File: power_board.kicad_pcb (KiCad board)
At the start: 2 copper layers, 141 x 90 mm, 172 parts, among them CON1 MICROUSB, J1 Conn_02x03_Odd_Even, J10 Conn_01x02, J11 Conn_01x02, J12 Conn_01x02, J13 Conn_01x02, J14 Conn_01x02, J15 Conn_01x02, J16 Conn_01x02, J17 Conn_01x02, J18 Conn_01x02, J19 Conn_01x02, J2 Conn_01x01, J20 Conn_01x02, J21 Conn_01x03, J22 Conn_01x03, J23 Conn_01x03, J24 Conn_01x03, J25 Conn_01x03, J26 Conn_01x02, J27 Conn_01x02, J28 Conn_01x02, J29 Conn_01x02, J3 Conn_01x01, J30 Conn_01x02, J31 Conn_01x02, J32 Conn_01x02, J33 Conn_01x02, J4 Conn_01x01, J5 ATX-24, J6 Conn_01x02, J7 Conn_01x02, J8 Conn_01x02, J9 Conn_01x02, K1 lsts-devices:RELAY_1RT, K2 lsts-devices:RELAY_1RT, K3 lsts-devices:RELAY_1RT, K4 lsts-devices:RELAY_1RT, K5 lsts-devices:RELAY_1RT, Q1 MMBT4401-7-F, Q10 MMBT4401-7-F, Q11 SI7113ADN-T1-GE3, Q12 MMBT4401-7-F, Q13 MMBT4401-7-F, Q14 MMBT4401-7-F, Q15 SI7113ADN-T1-GE3, Q16 SI7113ADN-T1-GE3, Q17 SI7113ADN-T1-GE3, Q18 MMBT4401-7-F, Q19 MMBT4401-7-F, Q2 MMBT4401-7-F, Q20 SI7113ADN-T1-GE3, Q21 SI7113ADN-T1-GE3, Q3 MMBT4401-7-F, Q4 SI7113ADN-T1-GE3, Q5 SI7113ADN-T1-GE3, Q6 MMBT4401-7-F, Q7 MMBT4401-7-F, Q8 SI7113ADN-T1-GE3, Q9 SI7113ADN-T1-GE3, SW1 SW_Push, U1 PCA9685PW, U10 DRV8801PWP, U11 DRV8801PWP, U12 DRV8801PWP, U2 ATMEGA328P-AU, U3 PCA9685PW, U4 FT232RL, U5 DRV8801PWP, U6 DRV8801PWP, U7 DRV8801PWP, U8 DRV8801PWP, U9 DRV8801PWP, Y1 Crystal

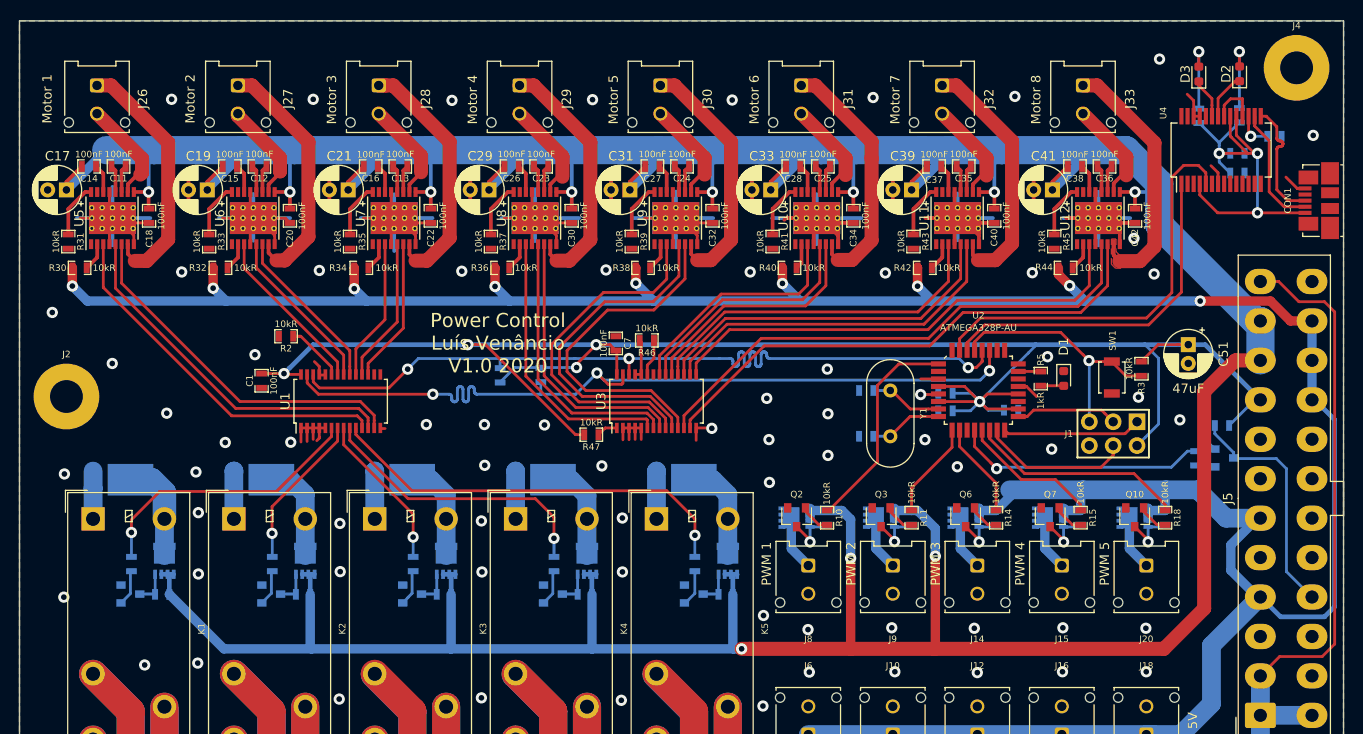
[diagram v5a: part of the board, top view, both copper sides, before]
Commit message: Replaced MCU by Arduino Nano
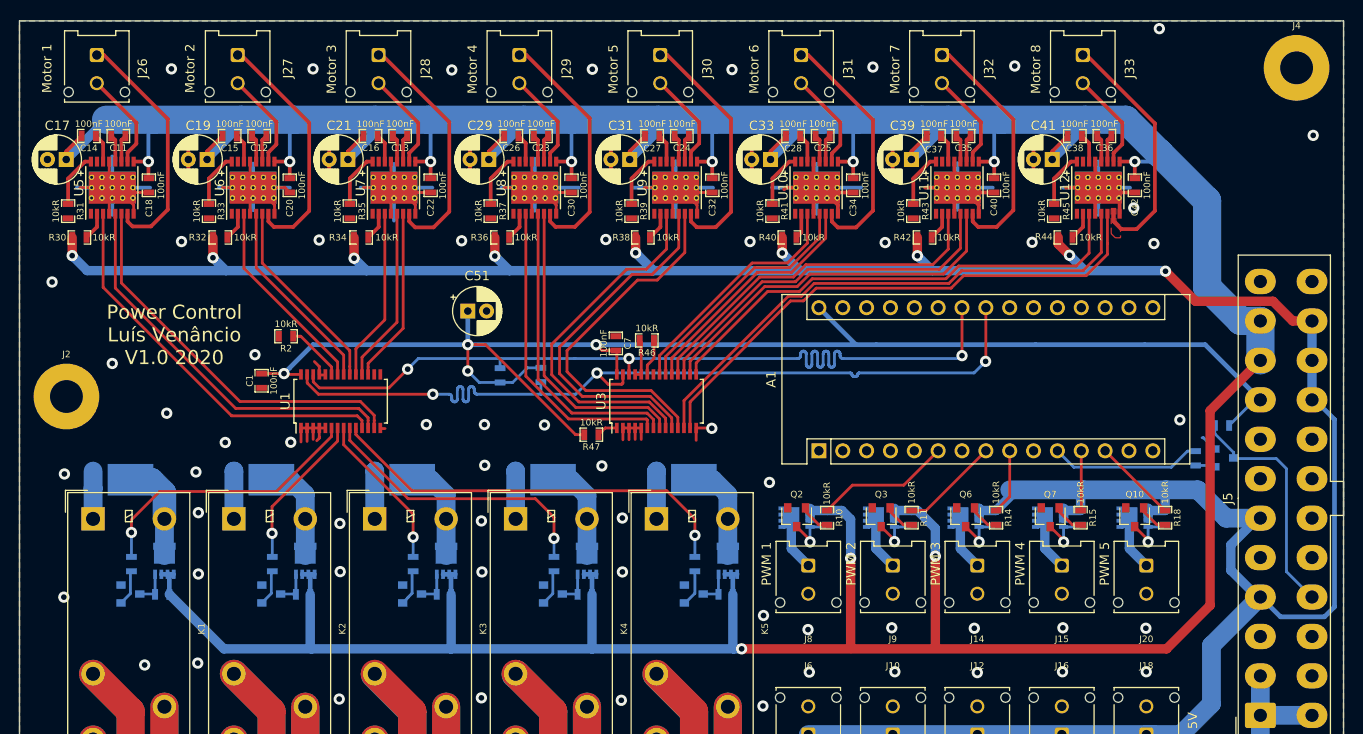
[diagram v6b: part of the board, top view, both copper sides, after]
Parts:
- removed C10, C2, C5, C6, C8, C9: 100nF, lsts-passives:C_0603
- removed C3, C4: 22nF, lsts-passives:C_0603
- removed CON1: MICROUSB, lsts-conn:USB_Micro-B_Molex_47346-0001
- removed D1, D2, D3: LED, LED_SMD:LED_0603_1608Metric
- removed J1: Conn_02x03_Odd_Even, lsts-conn:CONN_ISP
- removed R3: 10kR, lsts-passives:R_0603
- removed R5, R6, R7: 1kR, lsts-passives:R_0603
- removed SW1: SW_Push, Button_Switch_SMD:SW_SPST_B3U-1000P
- removed U2: ATMEGA328P-AU, lsts-ic:TQFP32
- removed U4: FT232RL, Package_SO:SSOP-28_5.3x10.2mm_P0.65mm
- removed Y1: Crystal, Crystal:Crystal_HC49-4H_Vertical
- added A1: Arduino_Nano_v3.x, Module:Arduino_Nano, F.Cu at (165.1, 105.8)
- moved C51 76.8 mm to (127.7, 90.9), turned to 0 degrees
- moved C11 3.24 mm to (90.5, 72.3)
- moved C12 3.24 mm to (105.5, 72.3)
- moved C13 3.24 mm to (120.5, 72.3)
- moved C14 3.24 mm to (87.4, 72.3)
- moved C15 3.24 mm to (102.4, 72.3)
- moved C16 3.24 mm to (117.4, 72.3)
- moved C17 3.24 mm to (85.0, 74.8)
- moved C18 3.24 mm to (93.8, 77.5)
- moved C19 3.24 mm to (100.0, 74.8)
- moved C20 3.24 mm to (108.8, 77.5)
- moved C21 3.24 mm to (115.0, 74.8)
- moved C22 3.24 mm to (123.8, 77.5)
- moved C23 3.24 mm to (135.5, 72.3)
- moved C24 3.24 mm to (150.5, 72.3)
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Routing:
- net +3V3: track 118.1 -> 64.1 mm
- net /+5V_SB: track 204.1 -> 158.6 mm, vias 5 -> 4
- net /5V_USB: track 44.1 -> 0.00 mm, vias 3 -> 0
- net /AT_TXD: track 43.8 -> 0.00 mm
- net /AT_RXD: track 37.4 -> 0.00 mm
- net /RESET: track 27.6 -> 0.00 mm, vias 1 -> 0
- net GND: track 342.9 -> 323.3 mm, vias 79 -> 68
- net /MOSI: track 16.0 -> 0.00 mm
- net /MISO: track 14.8 -> 0.00 mm
- net /PWM5_5V: track 23.1 -> 9.02 mm
- net /D-: track 13.2 -> 0.00 mm
- net /D+: track 13.2 -> 0.00 mm
- net /SCK: track 10.9 -> 0.00 mm
- net /PWR_CTR: track 27.0 -> 16.1 mm, vias 1 -> 0
- net /PWM4_5V: track 15.0 -> 6.39 mm
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
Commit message: Final touches
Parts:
- removed C28, C30, C32, C34, C35, C36, C37, C38, C40, C42: 100nF, lsts-passives:C_0603
- removed C29, C31, C33, C39, C41: 100uF, Capacitor_THT:CP_Radial_D5.0mm_P2.00mm
- removed D6, D7, D8: SDT5100LP5-13, Diode_SMD:D_PowerDI-5
- removed the J25 at (155.3, 146.6)
- removed J31, J32, J33: Conn_01x02, Connector_Molex:Molex_Micro-Fit_3.0_43045-0212_2x01_P3.00mm_Vertical
- removed Q17, Q20, Q21: SI7113ADN-T1-GE3, lsts-discretes:PowerPAK_1212-8
- removed Q18, Q19: MMBT4401-7-F, lsts-discretes:SOT23_BC817
- removed R42, R43, R44, R45, R46: 10kR, lsts-passives:R_0603
- removed U10, U11, U12, U9: DRV8801PWP, Package_SO:HTSSOP-16-1EP_4.4x5mm_P0.65mm_EP3.4x5mm_Mask3x3mm_ThermalVias
- added ?: , , F.Cu at (98.1, 64.9)
- added C10: 100uF, Capacitor_THT:CP_Radial_D5.0mm_P2.00mm, F.Cu at (99.9, 70.5)
- added C17: 100nF, lsts_passives:C_0603, F.Cu at (127.0, 70.5)
- added C4: 100nF, lsts_passives:C_0603, F.Cu at (81.7, 73.7)
- added C5: 100nF, lsts_passives:C_0603, F.Cu at (101.7, 73.7)
- added C6: 100nF, lsts_passives:C_0603, F.Cu at (81.7, 76.3)
- added C7: 100nF, lsts_passives:C_0603, F.Cu at (101.7, 76.3)
- added C9: 100nF, lsts_passives:C_0603, F.Cu at (87.0, 70.5)
- added D1: SDT5100LP5-13, Diode_SMD:D_PowerDI-5, B.Cu at (76.5, 113.0)
- added D2: SDT5100LP5-13, Diode_SMD:D_PowerDI-5, B.Cu at (94.0, 113.0)
- added D3: SDT5100LP5-13, Diode_SMD:D_PowerDI-5, B.Cu at (111.5, 113.0)
- added J20: Conn_01x03, TerminalBlock_Phoenix:TerminalBlock_Phoenix_PT-1,5-3-3.5-H_1x03_P3.50mm_Horizontal, F.Cu at (73.0, 144.0)
- added J26: Conn_01x02, Connector_Molex:Molex_Micro-Fit_3.0_43045-0212_2x01_P3.00mm_Vertical, F.Cu at (108.7, 65.3)
- added R4: 10kR, lsts_passives:R_0603, F.Cu at (126.0, 91.3)
- added R5: 10kR, lsts_passives:R_0603, F.Cu at (169.9, 86.8)
- added R7: 10kR, lsts_passives:R_0603, F.Cu at (169.9, 89.7)
- added U3: DRV8801PWP, Package_SO:HTSSOP-16-1EP_4.4x5mm_P0.65mm_EP3.4x5mm_Mask3x3mm_ThermalVias, F.Cu at (87.2, 74.3)
- added U4: DRV8801PWP, Package_SO:HTSSOP-16-1EP_4.4x5mm_P0.65mm_EP3.4x5mm_Mask3x3mm_ThermalVias, F.Cu at (107.2, 74.3)
- C1, C11, C12, C13, C14, C15, C20, C22, C23, C25, C27: footprint lsts-passives:C_0603 -> lsts_passives:C_0603
- C16, C18, C24, C26: value 100nF -> 100uF; footprint lsts-passives:C_0603 -> Capacitor_THT:CP_Radial_D5.0mm_P2.00mm
- C19, C21: value 100uF -> 100nF; footprint Capacitor_THT:CP_Radial_D5.0mm_P2.00mm -> lsts_passives:C_0603
- C2: renamed from C7; footprint lsts-passives:C_0603 -> lsts_passives:C_0603
- J1: renamed from J2; footprint lsts-mecanical:MountingHole_3.5mm_Pad -> lsts_mecanical:MountingHole_3.5mm_Pad
- J2: renamed from J3; footprint lsts-mecanical:MountingHole_3.5mm_Pad -> lsts_mecanical:MountingHole_3.5mm_Pad
- J3: renamed from J4; footprint lsts-mecanical:MountingHole_3.5mm_Pad -> lsts_mecanical:MountingHole_3.5mm_Pad
- K1, K2, K3, K4, K5: value lsts-devices:RELAY_1RT -> SANYOU_SRD_Form_C; footprint Relay_THT:Relay_SPDT_Panasonic_JW1_FormC_lsts -> Relay_THT:Relay_SPDT_SANYOU_SRD_Series_Form_C
- Q1, Q10, Q2, Q3, Q6, Q7: footprint lsts-discretes:SOT23_BC817 -> lsts_discretes:SOT23_BC817
- Q11, Q4, Q5, Q8, Q9: footprint lsts-discretes:PowerPAK_1212-8 -> lsts_discretes:PowerPAK_1212-8
- Q12, Q13, Q14: value MMBT4401-7-F -> Q_NMOS_GDS; footprint lsts-discretes:SOT23_BC817 -> Package_TO_SOT_SMD:TO-252-2; moved to F.Cu
- Q15, Q16: value SI7113ADN-T1-GE3 -> Q_NMOS_GDS; footprint lsts-discretes:PowerPAK_1212-8 -> Package_TO_SOT_SMD:TO-252-2; moved to F.Cu
- R1, R10, R11, R12, R13, R14, R15, R16, R17, R18, R19, R2, R30, R31, R32, R33, R34, R35, R36, R37, R38, R39, R40, R41, R8, R9: footprint lsts-passives:R_0603 -> lsts_passives:R_0603
- R20, R21: value 10kR -> 600R; footprint lsts-passives:R_0603 -> lsts_passives:R_0603; moved to F.Cu
- R22, R26, R27: value 10kR -> 60kR; footprint lsts-passives:R_0603 -> lsts_passives:R_0603; moved to F.Cu
- R23, R29: value 100kR -> 60kR; footprint lsts-passives:R_0603 -> lsts_passives:R_0603; moved to F.Cu
- R24, R25, R28: value 100kR -> 600R; footprint lsts-passives:R_0603 -> lsts_passives:R_0603; moved to F.Cu
- R3: renamed from R4; footprint lsts-passives:R_0603 -> lsts_passives:R_0603
- R6: renamed from R47; footprint lsts-passives:R_0603 -> lsts_passives:R_0603
- moved C3 71.2 mm to (197.7, 104.3), turned to 90 degrees
- moved C21 66.7 mm to (181.7, 73.7), turned to 270 degrees
- moved A1 57.6 mm to (110.0, 89.2), turned to 270 degrees
- moved C20 53.1 mm to (161.7, 73.7), turned to 270 degrees
- moved U8 52.4 mm to (187.2, 74.3), turned to 180 degrees
- moved C26 47.6 mm to (179.9, 70.5), turned to 180 degrees
- moved U7 47.4 mm to (167.2, 74.3), turned to 180 degrees
- moved C19 47.2 mm to (146.9, 70.5)
- moved C18 46.6 mm to (139.9, 70.5), turned to 180 degrees
- moved C23 46.4 mm to (181.7, 76.3), turned to 0 degrees
- moved U6 42.5 mm to (147.2, 74.3), turned to 180 degrees
- moved R22 41.7 mm to (80.5, 113.0)
- moved D5 41.0 mm to (146.5, 113.0)
- moved J30 40.5 mm to (188.7, 65.3), turned to 270 degrees
- moved C27 39.6 mm to (186.9, 70.5), turned to 180 degrees
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- renumbered C51 to C3, C17 to C8, J11 to J10, J12 to J11, J13 to J12, J14 to J13, J15 to J14, J16 to J15, J17 to J16, J18 to J17, J19 to J18, J20 to J19, J26 to J25, J5 to J4, J6 to J5, J7 to J6, J8 to J7, J9 to J8, J10 to J9, U3 to U2
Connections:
- A1 pad 12: /PWM4_5V -> Net-(A1-Pad12)
- A1 pad 13: /PWM5_5V -> Net-(A1-Pad13)
- A1 pad 6: /PWM1_5V -> Net-(A1-Pad6)
- A1 pad 8: /PWM2_5V -> Net-(A1-Pad8)
- A1 pad 9: /PWM3_5V -> Net-(A1-Pad9)
- C11 pad 1: Net-(C11-Pad1) -> GND
- C11 pad 2: Net-(C11-Pad2) -> +12V
- C16 pad 2: Net-(C16-Pad2) -> GND
- C18 pad 1: GND -> +12V
- C18 pad 2: +12V -> GND
- C19 pad 1: +12V -> GND
- C19 pad 2: GND -> +12V
- C20 pad 1: GND -> Net-(C20-Pad1)
- C20 pad 2: +12V -> Net-(C20-Pad2)
- C21 pad 1: +12V -> Net-(C21-Pad1)
- C21 pad 2: GND -> Net-(C21-Pad2)
- C22 pad 1: GND -> +12V
- C22 pad 2: +12V -> Net-(C22-Pad2)
- C23 pad 1: Net-(C23-Pad1) -> +12V
- C24 pad 1: Net-(C24-Pad1) -> +12V
- C24 pad 2: Net-(C24-Pad2) -> GND
- C25 pad 1: Net-(C25-Pad1) -> GND
- C25 pad 2: Net-(C25-Pad2) -> +12V
- C26 pad 2: Net-(C26-Pad2) -> GND
- C27 pad 1: +12V -> GND
- C27 pad 2: Net-(C27-Pad2) -> +12V
- D4 pad 1: Net-(D4-Pad1) -> +5V
- D4 pad 2: GND -> Net-(D4-Pad2)
- D5 pad 1: Net-(D5-Pad1) -> +5V
- D5 pad 2: GND -> Net-(D5-Pad2)
- J25 pad 1: Net-(J26-Pad1) -> Net-(J25-Pad1)
- J25 pad 2: Net-(J26-Pad2) -> Net-(J25-Pad2)
- K1 pad 1: GND -> Net-(J20-Pad2)
- K1 pad 2: Net-(J21-Pad2) -> Net-(D1-Pad2)
- K1 pad 3: Net-(J21-Pad3) -> Net-(J20-Pad1)
- K1 pad 4: Net-(J21-Pad1) -> Net-(J20-Pad3)
- K1 pad 5: Net-(D4-Pad1) -> +5V
- K2 pad 1: GND -> Net-(J21-Pad2)
- K2 pad 2: Net-(J22-Pad2) -> Net-(D2-Pad2)
- K2 pad 3: Net-(J22-Pad3) -> Net-(J21-Pad1)
- K2 pad 4: Net-(J22-Pad1) -> Net-(J21-Pad3)
- K2 pad 5: Net-(D5-Pad1) -> +5V
- K3 pad 1: GND -> Net-(J22-Pad2)
- K3 pad 2: Net-(J23-Pad2) -> Net-(D3-Pad2)
- K3 pad 3: Net-(J23-Pad3) -> Net-(J22-Pad1)
- K3 pad 4: Net-(J23-Pad1) -> Net-(J22-Pad3)
- K3 pad 5: Net-(D6-Pad1) -> +5V
- K4 pad 1: GND -> Net-(J23-Pad2)
- K4 pad 2: Net-(J24-Pad2) -> Net-(D4-Pad2)
- K4 pad 3: Net-(J24-Pad3) -> Net-(J23-Pad1)
- K4 pad 4: Net-(J24-Pad1) -> Net-(J23-Pad3)
- K4 pad 5: Net-(D7-Pad1) -> +5V
- K5 pad 1: GND -> Net-(J24-Pad2)
- K5 pad 2: Net-(J25-Pad2) -> Net-(D5-Pad2)
- K5 pad 3: Net-(J25-Pad3) -> Net-(J24-Pad1)
- K5 pad 4: Net-(J25-Pad1) -> Net-(J24-Pad3)
- K5 pad 5: Net-(D8-Pad1) -> +5V
- R20 pad 2: Net-(Q12-PadB) -> Net-(Q12-Pad1)
- R21 pad 2: Net-(Q13-PadB) -> Net-(Q13-Pad1)
- R22 pad 1: /RLY3_EN -> GND
- R22 pad 2: Net-(Q14-PadB) -> Net-(Q12-Pad1)
- R23 pad 1: Net-(Q12-PadC) -> GND
- R23 pad 2: +12V -> Net-(Q13-Pad1)
- R24 pad 1: Net-(Q13-PadC) -> /RLY3_EN
- R24 pad 2: +12V -> Net-(Q14-Pad1)
- R25 pad 1: Net-(Q14-PadC) -> /RLY4_EN
- R25 pad 2: +12V -> Net-(Q15-Pad1)
- R26 pad 1: /RLY4_EN -> GND
- R26 pad 2: Net-(Q18-PadB) -> Net-(Q14-Pad1)
- R27 pad 1: /RLY5_EN -> GND
- R27 pad 2: Net-(Q19-PadB) -> Net-(Q15-Pad1)
- R28 pad 1: Net-(Q18-PadC) -> /RLY5_EN
- R28 pad 2: +12V -> Net-(Q16-Pad1)
- R29 pad 1: Net-(Q19-PadC) -> GND
- R29 pad 2: +12V -> Net-(Q16-Pad1)
- U1 pad 11: /MTR1_PH -> /MTR3_PH
- U1 pad 12: /MTR1_SL -> /MTR3_SL
- U1 pad 13: /MTR1_EN -> /MTR3_EN
- U1 pad 17: /MTR3_EN -> /MTR2_EN
- U1 pad 18: /MTR3_SL -> /MTR2_SL
- U1 pad 19: /MTR3_PH -> /MTR2_PH
- U1 pad 20: /MTR2_EN -> /MTR1_EN
- U1 pad 21: /MTR2_SL -> /MTR1_SL
- U1 pad 22: /MTR2_PH -> /MTR1_PH
- U1 pad 24: GND -> Net-(R4-Pad1)
- U2 pad 10: /MTR5_SL -> /PWM2_5V
- U2 pad 11: /MTR5_EN -> /PWM3_5V
- U2 pad 12: /MTR8_SL -> /PWM4_5V
- U2 pad 13: /MTR8_EN -> /PWM5_5V
- U2 pad 15: /MTR8_PH -> /MTR6_EN
- U2 pad 16: /MTR7_EN -> /MTR6_SL
- U2 pad 17: /MTR7_SL -> /MTR6_PH
- U2 pad 18: /MTR7_PH -> /MTR5_EN
- U2 pad 19: /MTR6_EN -> /MTR5_SL
- U2 pad 20: /MTR6_SL -> /MTR5_PH
- U2 pad 21: /MTR6_PH -> Net-(U2-Pad21)
- U2 pad 24: GND -> Net-(R7-Pad1)
- U2 pad 9: /MTR5_PH -> /PWM1_5V
- U5 pad 10: Net-(J26-Pad2) -> Net-(J27-Pad2)
- U5 pad 11: Net-(C11-Pad1) -> Net-(C12-Pad1)
- U5 pad 12: Net-(C11-Pad2) -> Net-(C12-Pad2)
- U5 pad 16: Net-(R31-Pad1) -> Net-(R35-Pad1)
- U5 pad 2: Net-(R30-Pad2) -> Net-(R34-Pad2)
- U5 pad 3: /MTR1_PH -> /MTR3_PH
- U5 pad 5: /MTR1_SL -> /MTR3_SL
- U5 pad 6: /MTR1_EN -> /MTR3_EN
- U5 pad 7: Net-(J26-Pad1) -> Net-(J27-Pad1)
- U6 pad 10: Net-(J27-Pad2) -> Net-(J28-Pad2)
- U6 pad 11: Net-(C12-Pad1) -> Net-(C13-Pad1)
- U6 pad 12: Net-(C12-Pad2) -> Net-(C13-Pad2)
- U6 pad 16: Net-(R33-Pad1) -> Net-(R37-Pad1)
- U6 pad 2: Net-(R32-Pad2) -> Net-(R36-Pad2)
- U6 pad 3: /MTR2_PH -> /MTR4_PH
- U6 pad 5: /MTR2_SL -> /MTR4_SL
- U6 pad 6: /MTR2_EN -> /MTR4_EN
- U6 pad 7: Net-(J27-Pad1) -> Net-(J28-Pad1)
- U7 pad 10: Net-(J28-Pad2) -> Net-(J29-Pad2)
- U7 pad 11: Net-(C13-Pad1) -> Net-(C20-Pad1)
- U7 pad 12: Net-(C13-Pad2) -> Net-(C20-Pad2)
- U7 pad 14: Net-(C16-Pad2) -> Net-(C22-Pad2)
- U7 pad 16: Net-(R35-Pad1) -> Net-(R39-Pad1)
- U7 pad 2: Net-(R34-Pad2) -> Net-(R38-Pad2)
- U7 pad 3: /MTR3_PH -> /MTR5_PH
- U7 pad 5: /MTR3_SL -> /MTR5_SL
- U7 pad 6: /MTR3_EN -> /MTR5_EN
- U7 pad 7: Net-(J28-Pad1) -> Net-(J29-Pad1)
- U8 pad 10: Net-(J29-Pad2) -> Net-(J30-Pad2)
- U8 pad 11: Net-(C23-Pad1) -> Net-(C21-Pad1)
- U8 pad 12: Net-(C23-Pad2) -> Net-(C21-Pad2)
- U8 pad 14: Net-(C26-Pad2) -> Net-(C23-Pad2)
- U8 pad 16: Net-(R37-Pad1) -> Net-(R41-Pad1)
- U8 pad 2: Net-(R36-Pad2) -> Net-(R40-Pad2)
- U8 pad 3: /MTR4_PH -> /MTR6_PH
- U8 pad 5: /MTR4_SL -> /MTR6_SL
- U8 pad 6: /MTR4_EN -> /MTR6_EN
- U8 pad 7: Net-(J29-Pad1) -> Net-(J30-Pad1)
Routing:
- net +5V: track 321.2 -> 573.2 mm, vias 9 -> 7
- net GND: track 323.3 -> 132.2 mm, vias 68 -> 36
- net /PWR_CTR: track 16.1 -> 126.0 mm
- net +12V: track 498.5 -> 396.9 mm, vias 11 -> 8
- net /MTR8_EN: track 58.1 -> 0.00 mm
- net /MTR8_SL: track 58.0 -> 0.00 mm
- net /MTR8_PH: track 52.1 -> 0.00 mm
- net /MTR7_EN: track 39.7 -> 0.00 mm
- net /MTR7_SL: track 39.6 -> 0.00 mm
- net /MTR7_PH: track 39.1 -> 0.00 mm
- net Net-(J25-Pad2): track 37.5 -> 10.0 mm
- net Net-(J31-Pad1): track 26.4 -> 0.00 mm
- net Net-(J33-Pad1): track 26.4 -> 0.00 mm
- net /RLY1_EN: track 29.8 -> 56.0 mm, vias 1 -> 0
- net Net-(J32-Pad1): track 26.3 -> 0.00 mm
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- removed copper zone on F.Cu, net Net-(J33-Pad1)
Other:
- board size 141 x 90 mm -> 156 x 90 mm
- board text added: "Power Control Luís Venâncio V1.0 2021"
- board text removed: "Power Control Luís Venâncio V1.0 2020"

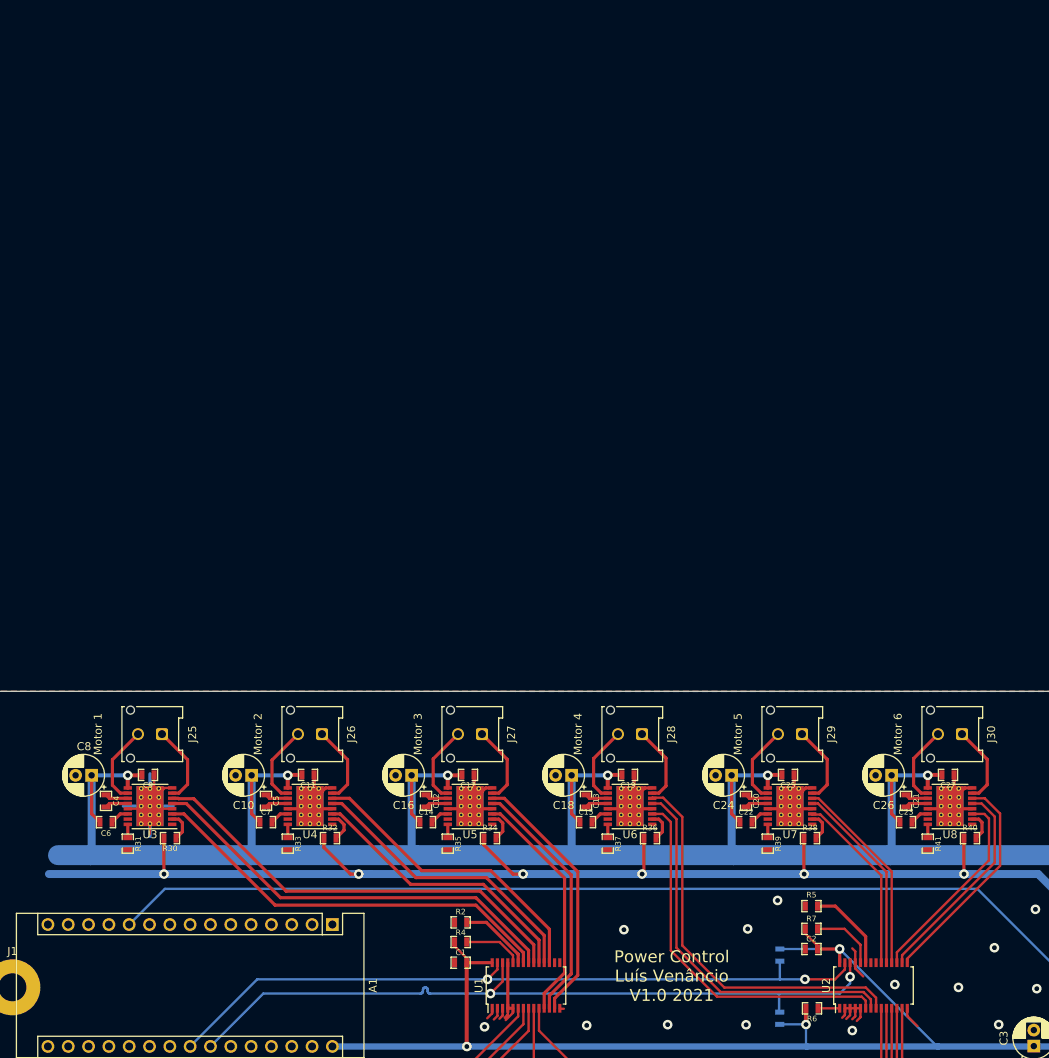
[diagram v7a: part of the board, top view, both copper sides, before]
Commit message: Replaced motor drivers
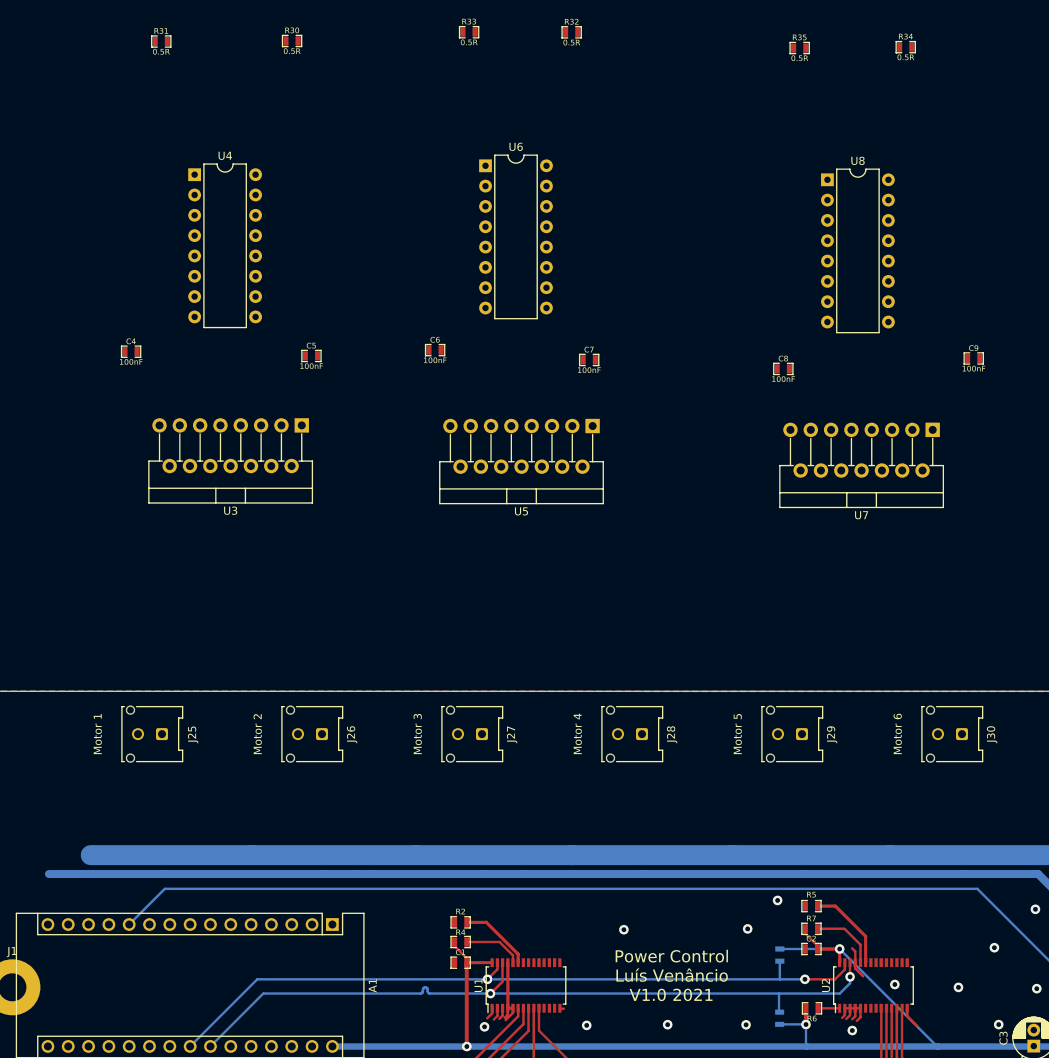
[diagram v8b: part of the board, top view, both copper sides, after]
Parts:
- removed C10, C16, C18, C24, C26: 100uF, Capacitor_THT:CP_Radial_D5.0mm_P2.00mm
- removed C11, C12, C13, C14, C15, C17, C19, C20, C21, C22, C23, C25, C27: 100nF, lsts_passives:C_0603
- removed R36, R37, R38, R39, R40, R41: 10kR, lsts_passives:R_0603
- C8: value 100uF -> 100nF; footprint Capacitor_THT:CP_Radial_D5.0mm_P2.00mm -> lsts_passives:C_0603
- R30, R31, R32, R33, R34, R35: value 10kR -> 0.5R
- U3, U5, U7: value DRV8801PWP -> L298HN; footprint Package_SO:HTSSOP-16-1EP_4.4x5mm_P0.65mm_EP3.4x5mm_Mask3x3mm_ThermalVias -> Package_TO_SOT_THT:TO-220-15_P2.54x2.54mm_StaggerOdd_Lead4.58mm_Vertical
- U4, U6, U8: value DRV8801PWP -> l6210; footprint Package_SO:HTSSOP-16-1EP_4.4x5mm_P0.65mm_EP3.4x5mm_Mask3x3mm_ThermalVias -> Package_DIP:DIP-16_W7.62mm
- moved C9 115.6 mm to (190.2, 18.4), turned to 0 degrees
- moved R34 111.7 mm to (181.7, -20.5)
- moved R35 108.8 mm to (168.4, -20.4), turned to 0 degrees
- moved R32 105.2 mm to (139.9, -22.4)
- moved R33 103.9 mm to (127.1, -22.4), turned to 0 degrees
- moved R30 100.8 mm to (105.0, -21.3)
- moved R31 100.4 mm to (88.6, -21.2), turned to 0 degrees
- moved C8 100.3 mm to (166.4, 19.7), turned to 0 degrees
- moved U6 82.1 mm to (129.1, -5.69), turned to 0 degrees
- moved U4 80.2 mm to (92.8, -4.58), turned to 0 degrees
- moved U8 79.8 mm to (171.9, -3.94), turned to 0 degrees
- moved C6 71.9 mm to (122.8, 17.4)
- moved C7 70.5 mm to (142.1, 18.6)
- moved C4 56.2 mm to (84.8, 17.6), turned to 0 degrees
- moved C5 55.9 mm to (107.4, 18.1), turned to 0 degrees
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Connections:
- C4 pad 1: Net-(C4-Pad1) -> +5V
- C4 pad 2: Net-(C4-Pad2) -> GND
- C5 pad 1: Net-(C5-Pad1) -> GND
- C5 pad 2: Net-(C5-Pad2) -> +12V
- C6 pad 1: +12V -> +5V
- C6 pad 2: Net-(C6-Pad2) -> GND
- C7 pad 1: +12V -> GND
- C7 pad 2: Net-(C7-Pad2) -> +12V
- C8 pad 1: +12V -> +5V
- R30 pad 1: +5V -> Net-(R30-Pad1)
- R30 pad 2: Net-(R30-Pad2) -> GND
- R32 pad 1: +5V -> Net-(R32-Pad1)
- R32 pad 2: Net-(R32-Pad2) -> GND
- R34 pad 1: +5V -> Net-(R34-Pad1)
- R34 pad 2: Net-(R34-Pad2) -> GND
- U1 pad 11: /MTR3_PH -> /MTR3_IN1
- U1 pad 12: /MTR3_SL -> /MTR3_IN2
- U1 pad 18: /MTR2_SL -> /MTR2_IN2
- U1 pad 19: /MTR2_PH -> /MTR2_IN1
- U1 pad 21: /MTR1_SL -> /MTR1_IN2
- U1 pad 22: /MTR1_PH -> /MTR1_IN1
- U2 pad 16: /MTR6_SL -> /MTR6_IN2
- U2 pad 17: /MTR6_PH -> /MTR6_IN1
- U2 pad 19: /MTR5_SL -> /MTR5_IN2
- U2 pad 20: /MTR5_PH -> /MTR5_IN1
- U2 pad 6: /MTR4_PH -> /MTR4_IN1
- U2 pad 7: /MTR4_SL -> /MTR4_IN2
- U3 pad 1: Net-(U3-Pad1) -> Net-(R30-Pad1)
- U3 pad 10: Net-(J25-Pad2) -> /MTR2_IN1
- U3 pad 11: Net-(C4-Pad1) -> /MTR2_EN
- U3 pad 12: Net-(C4-Pad2) -> /MTR2_IN2
- U3 pad 13: GND -> Net-(J26-Pad2)
- U3 pad 14: Net-(C6-Pad2) -> Net-(J26-Pad1)
- U3 pad 15: Net-(U3-Pad15) -> Net-(R31-Pad1)
- U3 pad 2: Net-(R30-Pad2) -> Net-(J25-Pad2)
- U3 pad 3: /MTR1_PH -> Net-(J25-Pad1)
- U3 pad 4: GND -> +12V
- U3 pad 5: /MTR1_SL -> /MTR1_IN1
- U3 pad 7: Net-(J25-Pad1) -> /MTR1_IN2
- U3 pad 9: +12V -> +5V
- U4 pad 1: Net-(U4-Pad1) -> +12V
- U4 pad 10: Net-(J26-Pad2) -> Net-(J25-Pad1)
- U4 pad 11: Net-(C5-Pad1) -> GND
- U4 pad 12: Net-(C5-Pad2) -> GND
- U4 pad 14: Net-(C7-Pad2) -> GND
- U4 pad 15: Net-(U4-Pad15) -> Net-(J25-Pad2)
- U4 pad 16: Net-(R33-Pad1) -> +12V
- U4 pad 2: Net-(R32-Pad2) -> Net-(J26-Pad2)
- U4 pad 3: /MTR2_PH -> GND
- U4 pad 5: /MTR2_SL -> GND
- U4 pad 6: /MTR2_EN -> GND
- U4 pad 8: GND -> +12V
- U5 pad 1: Net-(U5-Pad1) -> Net-(R32-Pad1)
- U5 pad 10: Net-(J27-Pad2) -> /MTR4_IN1
- U5 pad 11: Net-(C12-Pad1) -> /MTR4_EN
- U5 pad 12: Net-(C12-Pad2) -> /MTR4_IN2
- U5 pad 13: GND -> Net-(J28-Pad2)
- U5 pad 14: Net-(C14-Pad2) -> Net-(J28-Pad1)
- U5 pad 15: Net-(U5-Pad15) -> Net-(R33-Pad1)
- U5 pad 2: Net-(R34-Pad2) -> Net-(J27-Pad2)
- U5 pad 3: /MTR3_PH -> Net-(J27-Pad1)
- U5 pad 4: GND -> +12V
- U5 pad 5: /MTR3_SL -> /MTR3_IN1
- U5 pad 7: Net-(J27-Pad1) -> /MTR3_IN2
- U5 pad 9: +12V -> +5V
- U6 pad 1: Net-(U6-Pad1) -> +12V
- U6 pad 10: Net-(J28-Pad2) -> Net-(J27-Pad1)
- U6 pad 11: Net-(C13-Pad1) -> GND
- U6 pad 12: Net-(C13-Pad2) -> GND
- U6 pad 14: Net-(C15-Pad2) -> GND
- U6 pad 15: Net-(U6-Pad15) -> Net-(J27-Pad2)
- U6 pad 16: Net-(R37-Pad1) -> +12V
- U6 pad 2: Net-(R36-Pad2) -> Net-(J28-Pad2)
- U6 pad 3: /MTR4_PH -> GND
- U6 pad 5: /MTR4_SL -> GND
- U6 pad 6: /MTR4_EN -> GND
- U6 pad 8: GND -> +12V
- U7 pad 1: Net-(U7-Pad1) -> Net-(R34-Pad1)
- U7 pad 10: Net-(J29-Pad2) -> /MTR6_IN1
- U7 pad 11: Net-(C20-Pad1) -> /MTR6_EN
- U7 pad 12: Net-(C20-Pad2) -> /MTR6_IN2
- U7 pad 13: GND -> Net-(J30-Pad2)
- U7 pad 14: Net-(C22-Pad2) -> Net-(J30-Pad1)
- U7 pad 15: Net-(U7-Pad15) -> Net-(R35-Pad1)
- U7 pad 2: Net-(R38-Pad2) -> Net-(J29-Pad2)
- U7 pad 3: /MTR5_PH -> Net-(J29-Pad1)
- U7 pad 4: GND -> +12V
- U7 pad 5: /MTR5_SL -> /MTR5_IN1
- U7 pad 7: Net-(J29-Pad1) -> /MTR5_IN2
- U7 pad 9: +12V -> +5V
- U8 pad 1: Net-(U8-Pad1) -> +12V
- U8 pad 10: Net-(J30-Pad2) -> Net-(J29-Pad1)
- U8 pad 11: Net-(C21-Pad1) -> GND
- U8 pad 12: Net-(C21-Pad2) -> GND
- U8 pad 14: Net-(C23-Pad2) -> GND
- U8 pad 15: Net-(U8-Pad15) -> Net-(J29-Pad2)
- U8 pad 16: Net-(R41-Pad1) -> +12V
- U8 pad 2: Net-(R40-Pad2) -> Net-(J30-Pad2)
- U8 pad 3: /MTR6_PH -> GND
- U8 pad 5: /MTR6_SL -> GND
- U8 pad 6: /MTR6_EN -> GND
- U8 pad 8: GND -> +12V
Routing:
- net +12V: track 396.9 -> 248.3 mm, vias 8 -> 2
- net GND: track 132.2 -> 31.5 mm
- net /MTR1_EN: track 55.0 -> 0.00 mm
- net /MTR1_SL: track 53.7 -> 0.00 mm
- net /MTR1_PH: track 52.3 -> 0.00 mm
- net /MTR4_EN: track 49.1 -> 0.00 mm
- net /MTR4_SL: track 48.0 -> 0.00 mm
- net /MTR4_PH: track 46.7 -> 0.00 mm
- net /MTR2_EN: track 38.1 -> 0.00 mm
- net /MTR2_SL: track 36.7 -> 0.00 mm
- net /MTR2_PH: track 35.2 -> 0.00 mm
- net /MTR3_EN: track 32.8 -> 0.00 mm
- net +5V: track 573.2 -> 541.0 mm, vias 7 -> 1
- net /MTR3_SL: track 31.4 -> 0.00 mm
- net /MTR3_PH: track 29.7 -> 0.00 mm
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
